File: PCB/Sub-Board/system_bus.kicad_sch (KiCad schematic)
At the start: 1 part, among them J1 Conn_02x08_Row_Letter_Last

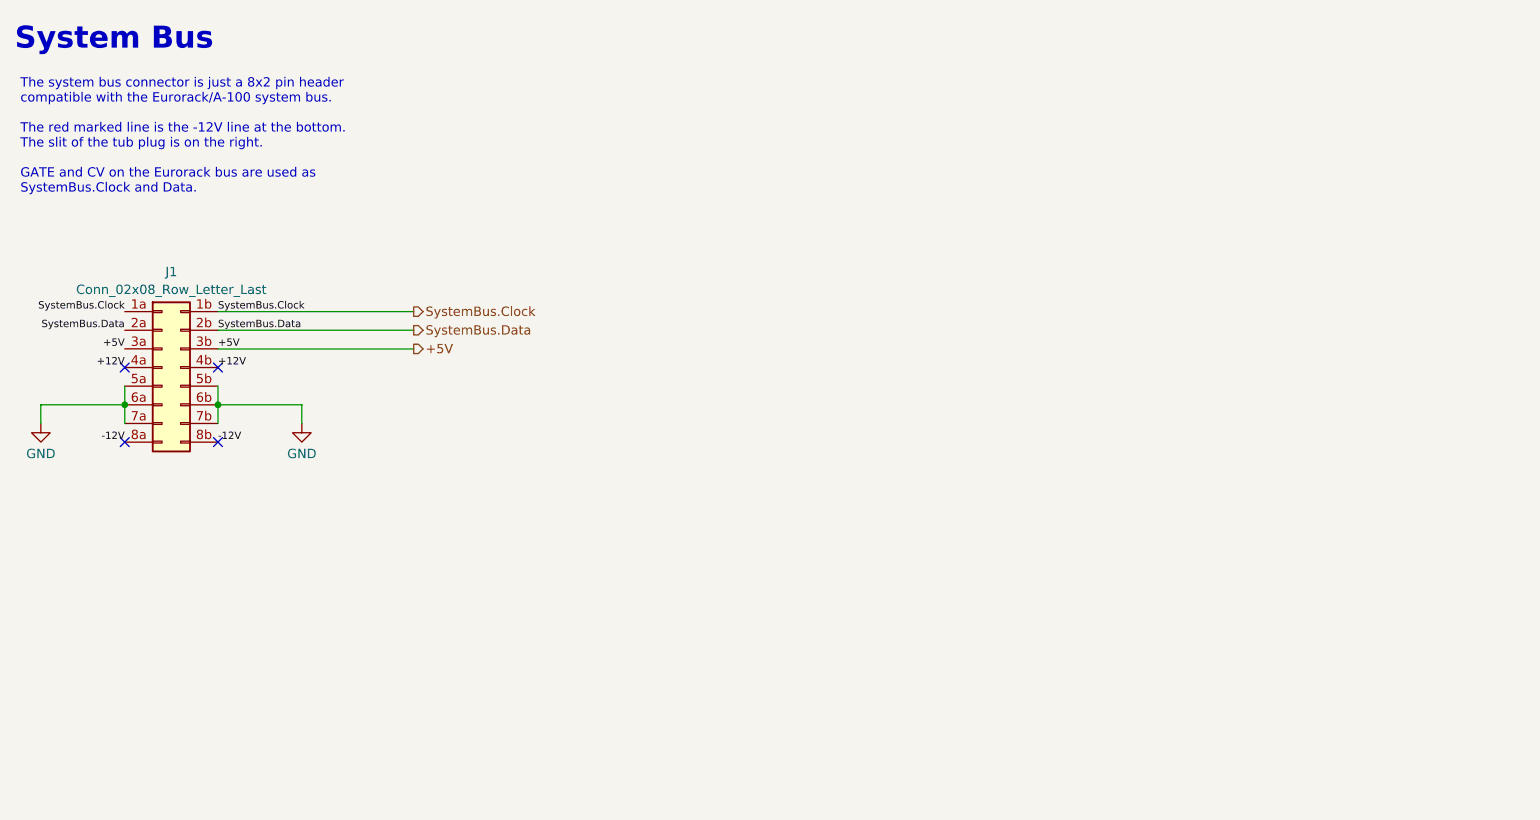
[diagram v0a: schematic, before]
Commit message: Sub-Board PCB before ERC
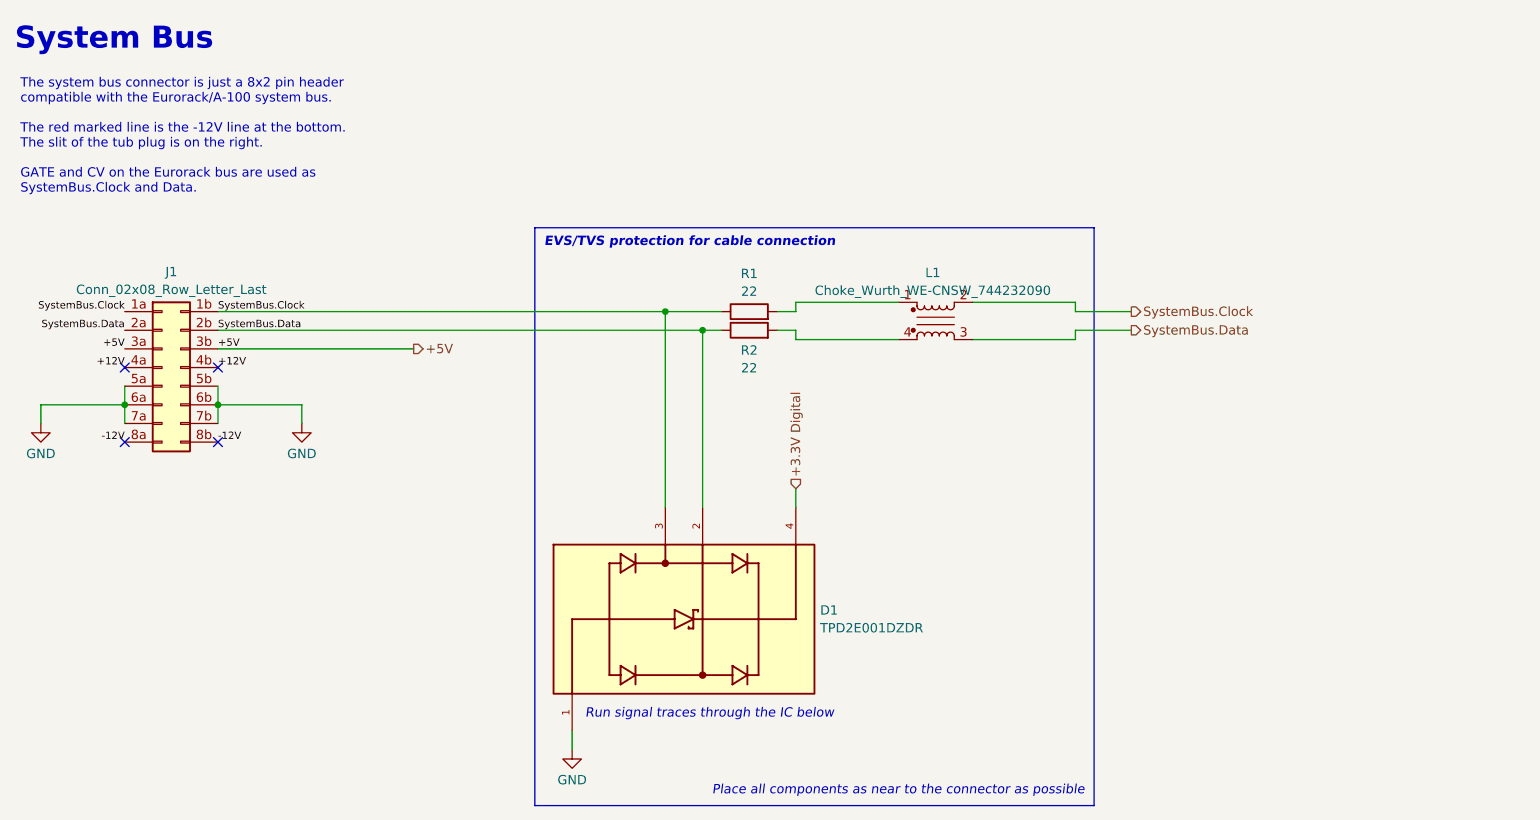
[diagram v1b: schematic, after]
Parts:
- added D1: TPD2E001DZDR, TPD2E001DZDR:SOT192P237X122-4N, symbol TPD2E001DZDR:TPD2E001DZDR
- added L1: Choke_Wurth_WE-CNSW_744232090, Inductor_SMD:L_CommonMode_Wurth_WE-CNSW-1206, symbol Filter:Choke_Wurth_WE-CNSW_744232090
- added R1, R2: 22, symbol Device:R
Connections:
- net GND: now also D1.1
- net SystemBus.Clock: now also D1.3, L1.2, R1.1
- net SystemBus.Data: now also D1.2, L1.3, R2.1
- new net: L1.4, R2.2
- new net: L1.1, R1.2
- new net +3.3V Digital: D1.4
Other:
- note added: "EVS/TVS protection for cable connection"
- note added: "Place all components as near to the connector as possible"
- note added: "Run signal traces through the IC below"

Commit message: Sub-Board PCB after ERC
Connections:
- no-connect marks 4 -> 0
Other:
- moved on the sheet: D1, J1, L1, R1, R2

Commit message: Sub-Board PCB: I2C Busses
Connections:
- net SystemBus.Clock: no longer D1.3, J1.1b (Pin_1b), R1.1
- net SystemBus.Data: no longer D1.2, J1.2b (Pin_2b), R2.1
- new net: D1.3, J1.1b (Pin_1b), R1.1
- new net: D1.2, J1.2b (Pin_2b), R2.1
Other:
- note added: "SystemBus.Clock"
- note added: "SystemBus.Data"
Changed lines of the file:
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@@
+		)
+	)
+	(text "SystemBus.Clock"
+		(exclude_from_sim no)
+		(at 86.36 64.77 0)
+		(effects
+			(font
+				(size 1 1)
+			)
+			(justify left bottom)
+		)
+	)
+	(text "SystemBus.Data"
+		(exclude_from_sim no)
+		(at 86.36 67.31 0)
+		(effects
+			(font
+				(size 1 1)
+			)
+			(justify left bottom)
 		)
 	)
@@
 		(color 0 0 0 0)
 	)
+	(bus_entry
+		(at 226.06 67.31)
+		(size 2.54 -2.54)
+		(stroke
+			(width 0)
+			(type default)
+		)
+	)
+	(bus_entry
+		(at 226.06 64.77)
+		(size 2.54 -2.54)
+		(stroke
+			(width 0)
+			(type default)
+		)
+	)
 	(wire
 		(pts
@@
 		)
 	)
-	(wire
-		(pts
-			(xy 203.2 63.5) (xy 203.2 64.77)
-		)
-		(stroke
-			(width 0)
-			(type default)
-		)
-	)
-	(wire
-		(pts
-			(xy 189.23 63.5) (xy 203.2 63.5)
+	(bus
+		(pts
+			(xy 228.6 57.15) (xy 228.6 62.23)
+		)
+		(stroke
+			(width 0)
+			(type default)
+		)
+	)
+	(wire
+		(pts
+			(xy 190.5 64.77) (xy 226.06 64.77)
 		)
 		(stroke
@@
 	(wire
 		(pts
-			(xy 165.1 68.58) (xy 179.07 68.58)
-		)
-		(stroke
-			(width 0)
-			(type default)
-		)
-	)
-	(wire
-		(pts
 			(xy 73.66 77.47) (xy 73.66 80.01)
 		)
@@
 	(wire
 		(pts
-			(xy 165.1 67.31) (xy 165.1 68.58)
-		)
-		(stroke
-			(width 0)
-			(type default)
-		)
-	)
-	(wire
-		(pts
-			(xy 165.1 63.5) (xy 179.07 63.5)
-		)
-		(stroke
-			(width 0)
-			(type default)
-		)
-	)
-	(wire
-		(pts
-			(xy 203.2 68.58) (xy 203.2 67.31)
-		)
-		(stroke
-			(width 0)
-			(type default)
-		)
-	)
-	(wire
-		(pts
-			(xy 162.56 64.77) (xy 165.1 64.77)
+			(xy 177.8 67.31) (xy 177.8 68.58)
+		)
+		(stroke
+			(width 0)
+			(type default)
+		)
+	)
+	(wire
+		(pts
+			(xy 162.56 64.77) (xy 177.8 64.77)
 		)
 		(stroke
@@
 	(wire
 		(pts
-			(xy 162.56 67.31) (xy 165.1 67.31)
-		)
-		(stroke
-			(width 0)
-			(type default)
-		)
-	)
-	(wire
-		(pts
-			(xy 165.1 64.77) (xy 165.1 63.5)
+			(xy 177.8 63.5) (xy 179.07 63.5)
+		)
+		(stroke
+			(width 0)
+			(type default)
+		)
+	)
+	(wire
+		(pts
+			(xy 162.56 67.31) (xy 177.8 67.31)
+		)
+		(stroke
+			(width 0)
+			(type default)
+		)
+	)
+	(bus
+		(pts
+			(xy 228.6 62.23) (xy 228.6 64.77)
+		)
+		(stroke
+			(width 0)
+			(type default)
+		)
+	)
+	(wire
+		(pts
+			(xy 190.5 67.31) (xy 190.5 68.58)
+		)
+		(stroke
+			(width 0)
+			(type default)
+		)
+	)
+	(wire
+		(pts
+			(xy 177.8 64.77) (xy 177.8 63.5)
 		)
 		(stroke
@@
 	(wire
 		(pts
+			(xy 190.5 64.77) (xy 190.5 63.5)
+		)
+		(stroke
+			(width 0)
+			(type default)
+		)
+	)
+	(wire
+		(pts
 			(xy 73.66 74.93) (xy 73.66 77.47)
 		)
@@
 	(wire
 		(pts
-			(xy 189.23 68.58) (xy 203.2 68.58)
-		)
-		(stroke
-			(width 0)
-			(type default)
-		)
-	)
-	(wire
-		(pts
-			(xy 203.2 67.31) (xy 210.82 67.31)
-		)
-		(stroke
-			(width 0)
-			(type default)
-		)
-	)
-	(wire
-		(pts
-			(xy 203.2 64.77) (xy 210.82 64.77)
+			(xy 190.5 67.31) (xy 226.06 67.31)
 		)
 		(stroke
@@
 	(wire
 		(pts
+			(xy 190.5 63.5) (xy 189.23 63.5)
+		)
+		(stroke
+			(width 0)
+			(type default)
+		)
+	)
+	(wire
+		(pts
 			(xy 165.1 88.9) (xy 165.1 91.44)
 		)
@@
 		(pts
 			(xy 152.4 67.31) (xy 152.4 91.44)
+		)
+		(stroke
+			(width 0)
+			(type default)
+		)
+	)
+	(wire
+		(pts
+			(xy 177.8 68.58) (xy 179.07 68.58)
+		)
+		(stroke
+			(width 0)
+			(type default)
+		)
+	)
+	(wire
+		(pts
+			(xy 190.5 68.58) (xy 189.23 68.58)
 		)
 		(stroke
@@
 		)
 	)
-	(label "SystemBus.Clock"
-		(at 86.36 64.77 0)
+	(label "SystemBus.Data"
+		(at 226.06 67.31 180)
 		(effects
 			(font
 				(size 1 1)
 			)
-			(justify left bottom)
+			(justify right bottom)
 		)
 	)
@@
 		)
 	)
+	(label "SystemBus.Clock"
+		(at 226.06 64.77 180)
+		(effects
+			(font
+				(size 1 1)
+			)
+			(justify right bottom)
+		)
+	)
 	(label "SystemBus.Data"
 		(at 73.66 67.31 180)
@@
 		)
 	)
-	(label "SystemBus.Data"
-		(at 86.36 67.31 0)
-		(effects
-			(font
-				(size 1 1)
-			)
-			(justify left bottom)
-		)
-	)
-	(hierarchical_label "SystemBus.Clock"
+	(hierarchical_label "SystemBus{I2C}"
 		(shape output)
-		(at 210.82 64.77 0)
-		(effects
-			(font
-				(size 1.27 1.27)
-			)
-			(justify left)
-		)
-	)
-	(hierarchical_label "SystemBus.Data"
-		(shape output)
-		(at 210.82 67.31 0)
+		(at 228.6 57.15 90)
 		(effects
 			(font
@@
 		(on_board yes)
 		(dnp no)
-		(fields_autoplaced yes)
 		(property "Reference" "L1"
-			(at 183.769 59.4825 0)
+			(at 184.15 58.0277 0)
 			(effects
 				(font
@@
 		)
 		(property "Value" "Choke_Wurth_WE-CNSW_744232090"
-			(at 183.769 61.9068 0)
-			(effects
-				(font
+			(at 184.15 60.452 0)
+			(effects
+				(font

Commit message: Sub-Board PCB: Footprint assignments
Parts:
- J1: footprint (none) -> Connector_PinHeader_2.54mm:PinHeader_2x08_P2.54mm_Horizontal
- R1, R2: footprint (none) -> Resistor_SMD:R_0603_1608Metric
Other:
- title: Modular Music Controller – System Bus -> Modular Music Controller / Sub-Board / System Bus
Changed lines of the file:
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@@
 	(paper "A4")
 	(title_block
-		(title "Modular Music Controller – System Bus")
+		(title "Modular Music Controller / Sub-Board / System Bus")
 		(date "2025-11-02")
 		(rev "1")
@@
 			)
 		)
-		(property "Footprint" ""
+		(property "Footprint" "Connector_PinHeader_2.54mm:PinHeader_2x08_P2.54mm_Horizontal"
 			(at 78.74 72.39 0)
 			(effects
@@
 			)
 		)
-		(property "Footprint" ""
+		(property "Footprint" "Resistor_SMD:R_0603_1608Metric"
 			(at 158.75 69.088 90)
 			(effects
@@
 			)
 		)
-		(property "Footprint" ""
+		(property "Footprint" "Resistor_SMD:R_0603_1608Metric"
 			(at 158.75 66.548 90)
 			(effects

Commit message: Sub Board PCB: PCB Layout (wip)
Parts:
- J1: value Conn_02x08_Row_Letter_Last -> Conn_02x08; footprint Connector_PinHeader_2.54mm:PinHeader_2x08_P2.54mm_Horizontal -> Connector_PinHeader_2.54mm:PinHeader_2x08_P2.54mm_Vertical_SMD; symbol Connector_Generic:Conn_02x08_Row_Letter_Last -> Connector_Generic:Conn_02x08_Odd_Even
- R1, R2: footprint Resistor_SMD:R_0603_1608Metric -> Resistor_SMD:R_0402_1005Metric
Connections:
- net +12V: now also J1.10 (Pin_10), J1.9 (Pin_9); no longer J1.4a (Pin_4a), J1.4b (Pin_4b)
- net +5V: now also J1.11 (Pin_11), J1.12 (Pin_12); no longer J1.3a (Pin_3a), J1.3b (Pin_3b)
- net -12V: now also J1.1 (Pin_1), J1.2 (Pin_2); no longer J1.8a (Pin_8a), J1.8b (Pin_8b)
- net GND: now also J1.3 (Pin_3), J1.4 (Pin_4), J1.5 (Pin_5), J1.6 (Pin_6), J1.7 (Pin_7), J1.8 (Pin_8); no longer J1.5a (Pin_5a), J1.5b (Pin_5b), J1.6a (Pin_6a), J1.6b (Pin_6b), J1.7a (Pin_7a), J1.7b (Pin_7b)
- net SystemBus.Clock: no longer J1.1a (Pin_1a)
- net SystemBus.Data: no longer J1.2a (Pin_2a)
- net SystemBus-Clock: now reaches D1.3, R1.1
- net SystemBus-Clock: now also J1.15 (Pin_15), J1.16 (Pin_16); no longer J1.1b (Pin_1b)
- net SystemBus-Data: now reaches D1.2, R2.1
- net SystemBus-Data: now also J1.13 (Pin_13), J1.14 (Pin_14); no longer J1.2b (Pin_2b)
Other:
- note removed: "SystemBus.Clock"
- note removed: "SystemBus.Data"
- moved on the sheet: J1

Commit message: Sub Board PCB: Parts Placement (wip)
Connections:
- net SystemBus-Clock: now also D1.2; no longer D1.3
- net SystemBus-Data: now also D1.3; no longer D1.2
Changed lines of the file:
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@@
 	)
 	(junction
-		(at 152.4 67.31)
+		(at 147.32 67.31)
 		(diameter 0)
 		(color 0 0 0 0)
@@
 	)
 	(junction
-		(at 147.32 64.77)
+		(at 152.4 64.77)
 		(diameter 0)
 		(color 0 0 0 0)
@@
 	(wire
 		(pts
-			(xy 86.36 67.31) (xy 152.4 67.31)
+			(xy 86.36 67.31) (xy 147.32 67.31)
+		)
+		(stroke
+			(width 0)
+			(type default)
+		)
+	)
+	(wire
+		(pts
+			(xy 147.32 67.31) (xy 147.32 91.44)
 		)
 		(stroke
@@
 	(wire
 		(pts
-			(xy 152.4 67.31) (xy 154.94 67.31)
-		)
-		(stroke
-			(width 0)
-			(type default)
-		)
-	)
-	(wire
-		(pts
 			(xy 177.8 63.5) (xy 179.07 63.5)
 		)
@@
 	(wire
 		(pts
-			(xy 147.32 64.77) (xy 154.94 64.77)
-		)
-		(stroke
-			(width 0)
-			(type default)
-		)
-	)
-	(wire
-		(pts
 			(xy 97.79 80.01) (xy 97.79 77.47)
 		)
@@
 	(wire
 		(pts
-			(xy 86.36 64.77) (xy 147.32 64.77)
+			(xy 86.36 64.77) (xy 152.4 64.77)
 		)
 		(stroke
@@
 	(wire
 		(pts
-			(xy 152.4 67.31) (xy 152.4 91.44)
+			(xy 147.32 67.31) (xy 154.94 67.31)
+		)
+		(stroke
+			(width 0)
+			(type default)
+		)
+	)
+	(wire
+		(pts
+			(xy 152.4 64.77) (xy 152.4 91.44)
 		)
 		(stroke
@@
 	(wire
 		(pts
+			(xy 152.4 64.77) (xy 154.94 64.77)
+		)
+		(stroke
+			(width 0)
+			(type default)
+		)
+	)
+	(wire
+		(pts
 			(xy 54.61 72.39) (xy 73.66 72.39)
 		)
@@
 		)
 		(stroke
-			(width 0)
-			(type default)
-		)
-	)
-	(wire
-		(pts
-			(xy 147.32 64.77) (xy 147.32 91.44)
-		)
-		(stroke

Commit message: Sub Board PCB: Routing (wip)
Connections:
- net SystemBus.Clock: now also L1.3; no longer L1.2
- net SystemBus.Data: now also L1.2; no longer L1.3
- net at R2.2: now also L1.1; no longer L1.4
- net at R1.2: now also L1.4; no longer L1.1
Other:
- note removed: "Run signal traces through the IC below"
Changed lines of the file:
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@@
-		)
-	)
-	(text "Run signal traces through the IC below"
-		(exclude_from_sim no)
-		(at 136.398 118.872 0)
-		(effects
-			(font
-				(size 1.27 1.27)
-				(italic yes)
-			)
-			(justify left top)
 		)
 	)
@@
 		(lib_id "Filter:Choke_Wurth_WE-CNSW_744232090")
 		(at 184.15 66.04 0)
+		(mirror x)
 		(unit 1)
 		(exclude_from_sim no)
@@
 		(dnp no)
 		(property "Reference" "L1"
-			(at 184.15 58.0277 0)
+			(at 184.15 61.0983 0)
 			(effects
 				(font
@@
 		)
 		(property "Value" "Choke_Wurth_WE-CNSW_744232090"
-			(at 184.15 60.452 0)
+			(at 184.15 58.674 0)
 			(effects
 				(font
@@
 		)
 		(property "Footprint" "Inductor_SMD:L_CommonMode_Wurth_WE-CNSW-1206"
-			(at 184.15 76.2 0)
+			(at 184.15 55.88 0)
 			(effects
 				(font
@@
 		)
 		(property "Datasheet" "https://www.we-online.com/components/products/datasheet/744232090.pdf"
-			(at 184.15 73.66 0)
-			(effects
-				(font
+			(at 184.15 58.42 0)
+			(effects
+				(font
